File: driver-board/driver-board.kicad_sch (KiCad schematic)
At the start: 50 parts, among them J1 MCP4725, J2 Conn_Coaxial, J3 MCP4725, J4 Conn_Coaxial, SW1 RST, SW2 BIAS ON/OF, U1 Pico, U2 MIC5317, U3 TSV358, U4 TSV358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

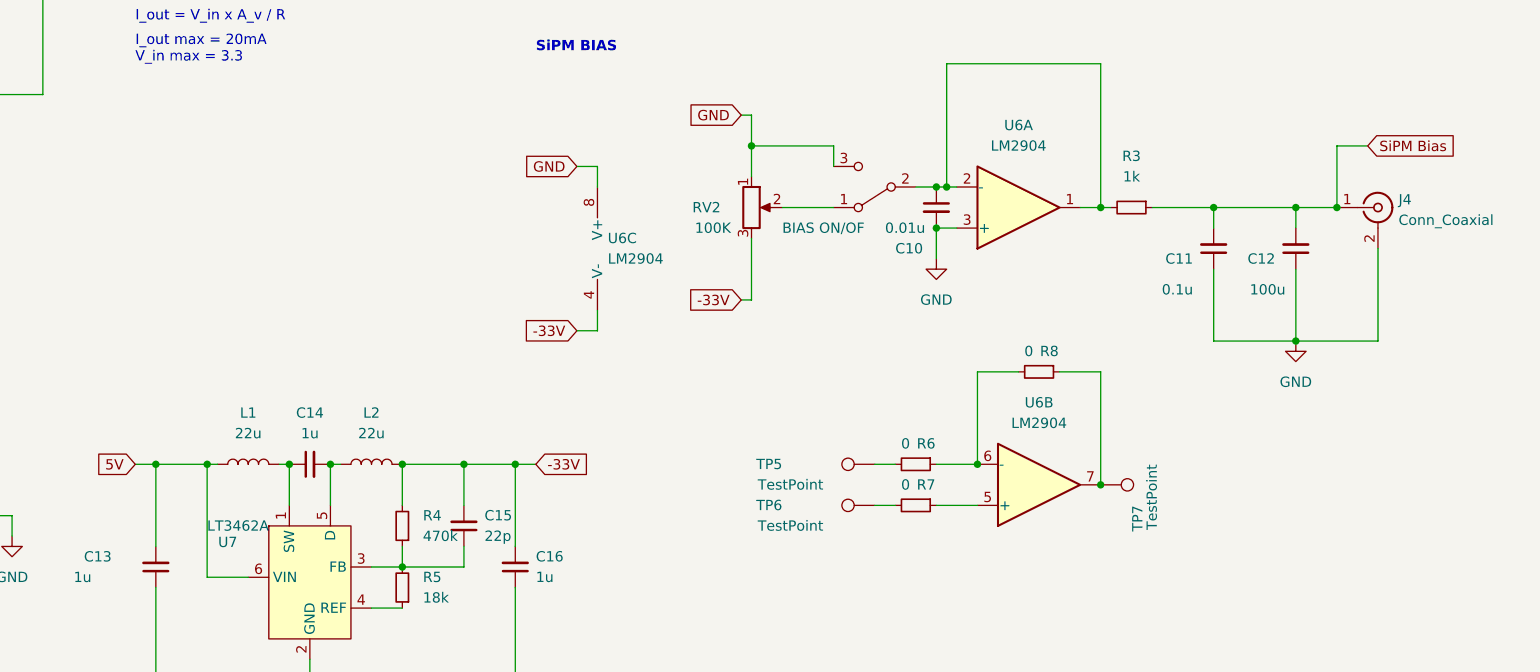
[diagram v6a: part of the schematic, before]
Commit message: Board reviewed, silk screen fixes
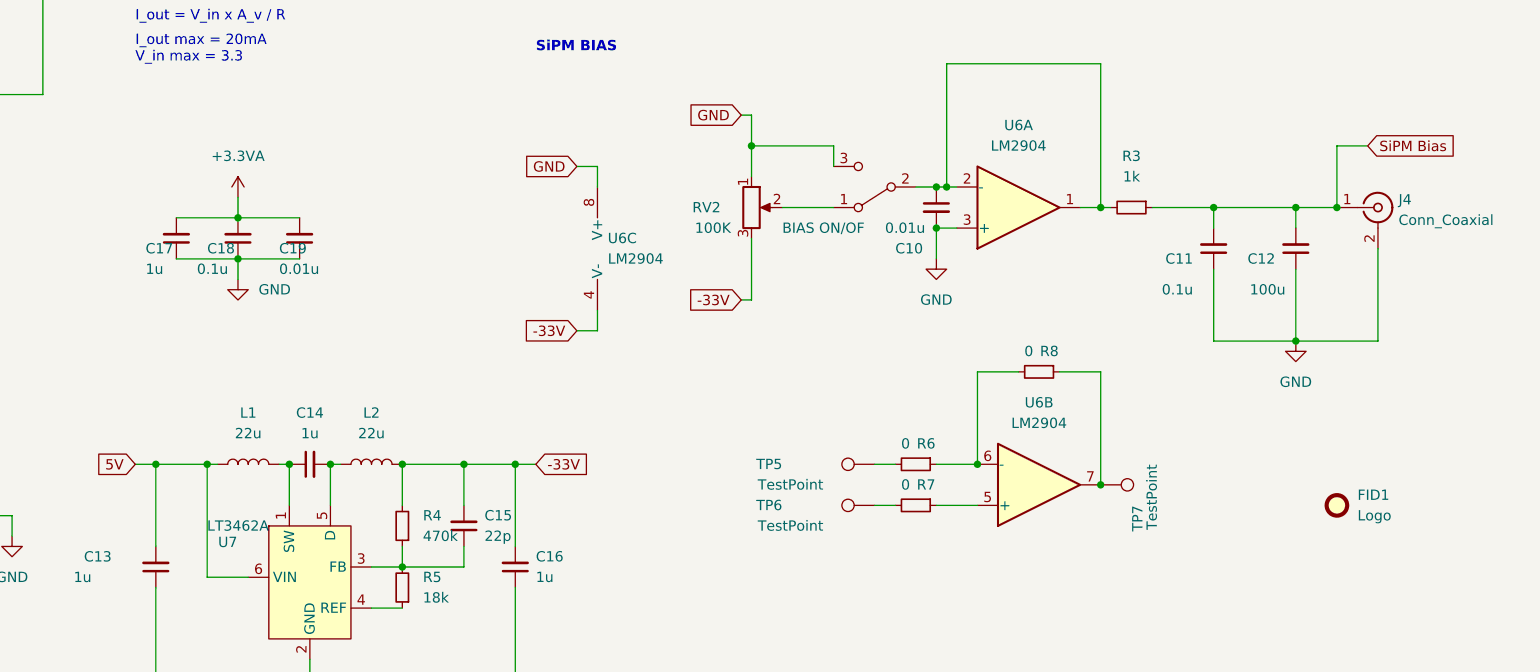
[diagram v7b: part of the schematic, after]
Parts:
- added C17: 1u, Capacitor_SMD:C_0805_2012Metric_Pad1.18x1.45mm_HandSolder, symbol Device:C_Small
- added C18: 0.1u, Capacitor_SMD:C_0805_2012Metric_Pad1.18x1.45mm_HandSolder, symbol Device:C_Small
- added C19: 0.01u, Capacitor_SMD:C_0805_2012Metric_Pad1.18x1.45mm_HandSolder, symbol Device:C_Small
- added FID1: Logo, lib:mendi-logo-plain, symbol Mechanical:Fiducial
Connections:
- net +3.3VA: now also C17.2, C18.2, C19.2
- net GND: now also C17.1, C18.1, C19.1
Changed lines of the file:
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@@
   (junction (at 158.75 153.67) (diameter 0) (color 0 0 0 0)
   )
+  (junction (at 130.81 128.27) (diameter 0) (color 0 0 0 0)
+  )
   (junction (at 139.7 180.34) (diameter 0) (color 0 0 0 0)
   )
@@
   )
   (junction (at 127 153.67) (diameter 0) (color 0 0 0 0)
+  )
+  (junction (at 130.81 123.19) (diameter 0) (color 0 0 0 0)
   )
   (junction (at 113.03 95.25) (diameter 0) (color 0 0 0 0)
@@
     (stroke (width 0) (type default) (color 0 0 0 0))
   )
+  (wire (pts (xy 123.19 128.27) (xy 130.81 128.27))
+    (stroke (width 0) (type default) (color 0 0 0 0))
+  )
   (wire (pts (xy 217.17 124.46) (xy 219.71 124.46))
     (stroke (width 0) (type default) (color 0 0 0 0))
@@
     (stroke (width 0) (type default) (color 0 0 0 0))
   )
+  (wire (pts (xy 130.81 128.27) (xy 138.43 128.27))
+    (stroke (width 0) (type default) (color 0 0 0 0))
+  )
   (wire (pts (xy 74.93 45.72) (xy 82.55 45.72))
     (stroke (width 0) (type default) (color 0 0 0 0))
@@
     (stroke (width 0) (type default) (color 0 0 0 0))
   )
+  (wire (pts (xy 130.81 123.19) (xy 138.43 123.19))
+    (stroke (width 0) (type default) (color 0 0 0 0))
+  )
   (wire (pts (xy 251.46 33.02) (xy 261.62 33.02))
     (stroke (width 0) (type default) (color 0 0 0 0))
@@
     (stroke (width 0) (type default) (color 0 0 0 0))
   )
+  (wire (pts (xy 130.81 120.65) (xy 130.81 123.19))
+    (stroke (width 0) (type default) (color 0 0 0 0))
+  )
   (wire (pts (xy 69.85 97.79) (xy 76.2 97.79))
     (stroke (width 0) (type default) (color 0 0 0 0))
@@
     (stroke (width 0) (type default) (color 0 0 0 0))
   )
+  (wire (pts (xy 130.81 128.27) (xy 130.81 130.81))
+    (stroke (width 0) (type default) (color 0 0 0 0))
+  )
   (wire (pts (xy 66.04 45.72) (xy 66.04 40.64))
     (stroke (width 0) (type default) (color 0 0 0 0))
@@
   )
   (wire (pts (xy 158.75 166.37) (xy 151.13 166.37))
+    (stroke (width 0) (type default) (color 0 0 0 0))
+  )
+  (wire (pts (xy 123.19 123.19) (xy 130.81 123.19))
     (stroke (width 0) (type default) (color 0 0 0 0))
   )
@@
     (pin "2")
   )
+  (symbol (lib_id "Device:C_Small") (at 123.19 125.73 180) (unit 1)
+    (in_bom yes) (on_board yes)
+    (property "Reference" "C17" (id 0) (at 119.38 127 0)
+      (effects (font (size 1.27 1.27)) (justify right))
+    )
+    (property "Value" "1u" (id 1) (at 119.38 129.54 0)
+      (effects (font (size 1.27 1.27)) (justify right))
+    )
+    (property "Footprint" "Capacitor_SMD:C_0805_2012Metric_Pad1.18x1.45mm_HandSolder" (id 2) (at 123.19 125.73 0)
+      (effects (font (size 1.27 1.27)) hide)
+    )
+    (property "Datasheet" "~" (id 3) (at 123.19 125.73 0)
+      (effects (font (size 1.27 1.27)) hide)
+    )
+    (pin "1")
+    (pin "2")
+  )
   (symbol (lib_id "Connector:TestPoint") (at 237.49 156.21 270) (unit 1)
     (in_bom yes) (on_board yes)
@@
     (pin "2")
   )
+  (symbol (lib_id "Device:C_Small") (at 130.81 125.73 180) (unit 1)
+    (in_bom yes) (on_board yes)
+    (property "Reference" "C18" (id 0) (at 127 127 0)
+      (effects (font (size 1.27 1.27)) (justify right))
+    )
+    (property "Value" "0.1u" (id 1) (at 125.73 129.54 0)
+      (effects (font (size 1.27 1.27)) (justify right))
+    )
+    (property "Footprint" "Capacitor_SMD:C_0805_2012Metric_Pad1.18x1.45mm_HandSolder" (id 2) (at 130.81 125.73 0)
+      (effects (font (size 1.27 1.27)) hide)
+    )
+    (property "Datasheet" "~" (id 3) (at 130.81 125.73 0)
+      (effects (font (size 1.27 1.27)) hide)
+    )
+    (pin "1")
+    (pin "2")
+  )
   (symbol (lib_id "Device:R_Small") (at 241.3 121.92 270) (unit 1)
     (in_bom yes) (on_board yes) (fields_autoplaced)
@@
     (pin "2")
   )
+  (symbol (lib_id "power:GND") (at 130.81 130.81 0) (mirror y) (unit 1)
+    (in_bom yes) (on_board yes) (fields_autoplaced)
+    (property "Reference" "#PWR015" (id 0) (at 130.81 137.16 0)
+      (effects (font (size 1.27 1.27)) hide)
+    )
+    (property "Value" "GND" (id 1) (at 133.35 132.0799 0)
+      (effects (font (size 1.27 1.27)) (justify right))
+    )
+    (property "Footprint" "" (id 2) (at 130.81 130.81 0)
+      (effects (font (size 1.27 1.27)) hide)
+    )
+    (property "Datasheet" "" (id 3) (at 130.81 130.81 0)
+      (effects (font (size 1.27 1.27)) hide)
+    )
+    (pin "1")
+  )
   (symbol (lib_id "fd-fnir:TSV358") (at 86.36 110.49 0) (mirror y) (unit 2)
     (in_bom yes) (on_board yes)
@@
     )
     (property "Datasheet" "~" (id 3) (at 209.55 153.67 0)
+      (effects (font (size 1.27 1.27)) hide)
+    )
+    (pin "1")
+  )
+  (symbol (lib_id "power:+3.3VA") (at 130.81 120.65 0) (unit 1)
+    (in_bom yes) (on_board yes) (fields_autoplaced)
+    (property "Reference" "#PWR014" (id 0) (at 130.81 124.46 0)
+      (effects (font (size 1.27 1.27)) hide)
+    )
+    (property "Value" "+3.3VA" (id 1) (at 130.81 115.57 0))
+    (property "Footprint" "" (id 2) (at 130.81 120.65 0)
+      (effects (font (size 1.27 1.27)) hide)
+    )
+    (property "Datasheet" "" (id 3) (at 130.81 120.65 0)
       (effects (font (size 1.27 1.27)) hide)
     )
@@
     (pin "1")
   )
+  (symbol (lib_id "Mechanical:Fiducial") (at 266.7 158.75 0) (unit 1)
+    (in_bom yes) (on_board yes) (fields_autoplaced)
+    (property "Reference" "FID1" (id 0) (at 269.24 157.4799 0)
+      (effects (font (size 1.27 1.27)) (justify left))
+    )
+    (property "Value" "Logo" (id 1) (at 269.24 160.0199 0)
+      (effects (font (size 1.27 1.27)) (justify left))
+    )
+    (property "Footprint" "lib:mendi-logo-plain" (id 2) (at 266.7 158.75 0)
+      (effects (font (size 1.27 1.27)) hide)
+    )
+    (property "Datasheet" "~" (id 3) (at 266.7 158.75 0)
+      (effects (font (size 1.27 1.27)) hide)
+    )
+  )
   (symbol (lib_id "Connector:Conn_01x06_Female") (at 24.13 86.36 0) (mirror y) (unit 1)
     (in_bom yes) (on_board yes) (fields_autoplaced)
@@
     (pin "1")
   )
+  (symbol (lib_id "Device:C_Small") (at 138.43 125.73 180) (unit 1)
+    (in_bom yes) (on_board yes)
+    (property "Reference" "C19" (id 0) (at 135.89 127 0)
+      (effects (font (size 1.27 1.27)) (justify right))
+    )
+    (property "Value" "0.01u" (id 1) (at 135.89 129.54 0)
+      (effects (font (size 1.27 1.27)) (justify right))
+    )
+    (property "Footprint" "Capacitor_SMD:C_0805_2012Metric_Pad1.18x1.45mm_HandSolder" (id 2) (at 138.43 125.73 0)
+      (effects (font (size 1.27 1.27)) hide)
+    )
+    (property "Datasheet" "~" (id 3) (at 138.43 125.73 0)
+      (effects (font (size 1.27 1.27)) hide)
+    )
+    (pin "1")
+    (pin "2")
+  )
   (symbol (lib_id "Amplifier_Operational:LM2904") (at 227.33 121.92 0) (mirror x) (unit 1)
     (in_bom yes) (on_board yes) (fields_autoplaced)
@@
       (reference "#PWR013") (unit 1) (value "+3.3VA") (footprint "")
     )
+    (path "/b3b6501e-8dcd-48dc-b603-15e8815305f4"
+      (reference "#PWR014") (unit 1) (value "+3.3VA") (footprint "")
+    )
+    (path "/a66fbdea-ac20-4e63-93a8-3fe0b5003205"
+      (reference "#PWR015") (unit 1) (value "GND") (footprint "")
+    )
     (path "/8ddca3dd-d4a0-4566-872c-8d67287506b9"
       (reference "#PWR0101") (unit 1) (value "GND") (footprint "")
@@
       (reference "C16") (unit 1) (value "1u") (footprint "Capacitor_SMD:C_0805_2012Metric_Pad1.18x1.45mm_HandSolder")
     )
+    (path "/4eb3d137-c3a0-4ced-8508-897e6609d25f"
+      (reference "C17") (unit 1) (value "1u") (footprint "Capacitor_SMD:C_0805_2012Metric_Pad1.18x1.45mm_HandSolder")
+    )
+    (path "/99b68cdc-697a-48e8-9b7a-50bff04d1ab6"
+      (reference "C18") (unit 1) (value "0.1u") (footprint "Capacitor_SMD:C_0805_2012Metric_Pad1.18x1.45mm_HandSolder")
+    )
+    (path "/fa1d3d41-de91-4607-87ae-3b485de979cc"
+      (reference "C19") (unit 1) (value "0.01u") (footprint "Capacitor_SMD:C_0805_2012Metric_Pad1.18x1.45mm_HandSolder")
+    )
+    (path "/d5ef2908-ba1b-40b9-a0ef-4455eb891bf6"
+      (reference "FID1") (unit 1) (value "Logo") (footprint "lib:mendi-logo-plain")
+    )
     (path "/dabde701-83b7-4ff8-b884-85a7bd4d4a26"

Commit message: added bom and pico code
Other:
- title: (none) -> FD-fNIRS
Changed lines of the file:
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@@
 (kicad_sch (version 20211123) (generator eeschema)
   (paper "A4")
+  (title_block
+    (title "FD-fNIRS")
+    (date "2022-03-18")
+    (rev "1")
+    (comment 1 "rohitrathnam.n@gmail.com")
+    (comment 2 "Rohit Rathnam Nareshkumar")
+  )
   (junction (at 217.17 124.46) (diameter 0) (color 0 0 0 0)
   )
